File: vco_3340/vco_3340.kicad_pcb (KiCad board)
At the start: 2 copper layers, 55 x 95 mm, 44 parts, among them J1 cv1, J2 cv2, J3 FM in, J4 PWM, J5 Sync In, J6 Power In, J7 Pulse Out, J8 Saw Out, J9 Tri Out, U1 TL072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

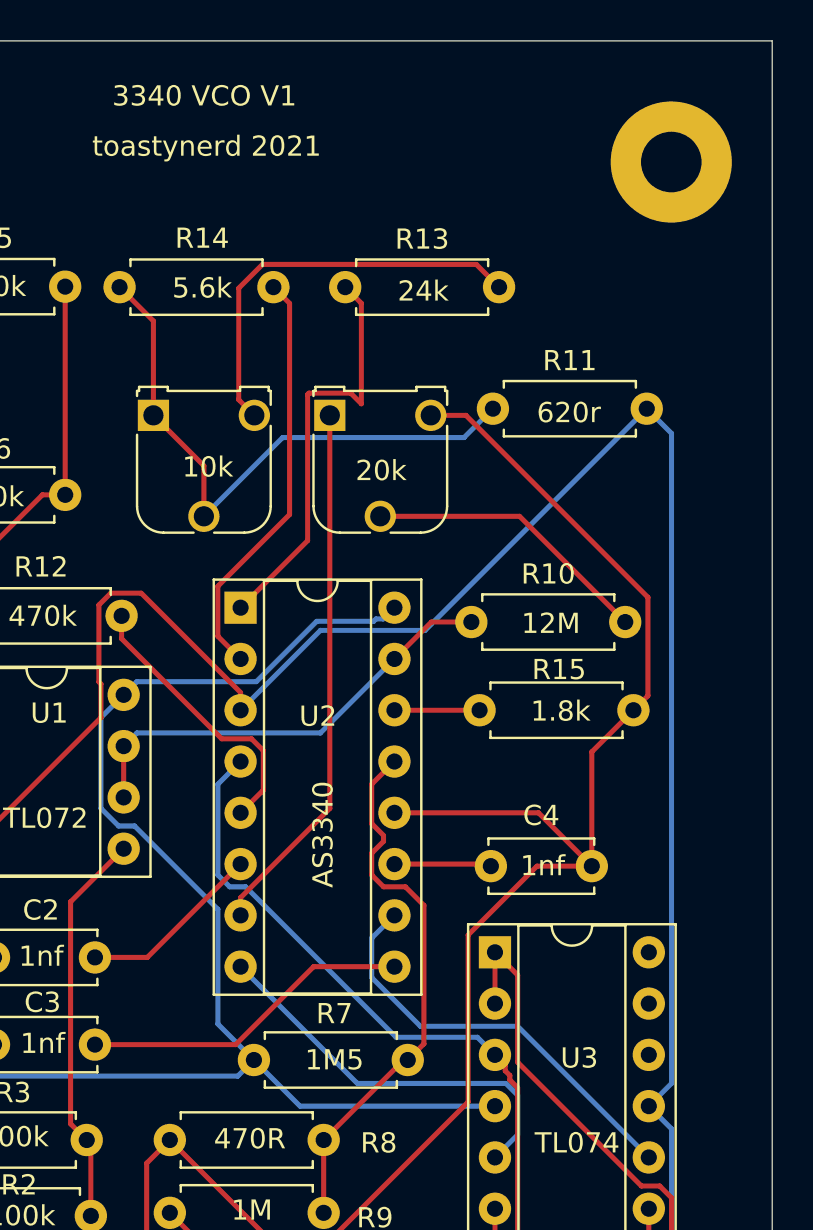
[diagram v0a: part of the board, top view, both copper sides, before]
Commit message: 3360 stencil and 3340 fixes
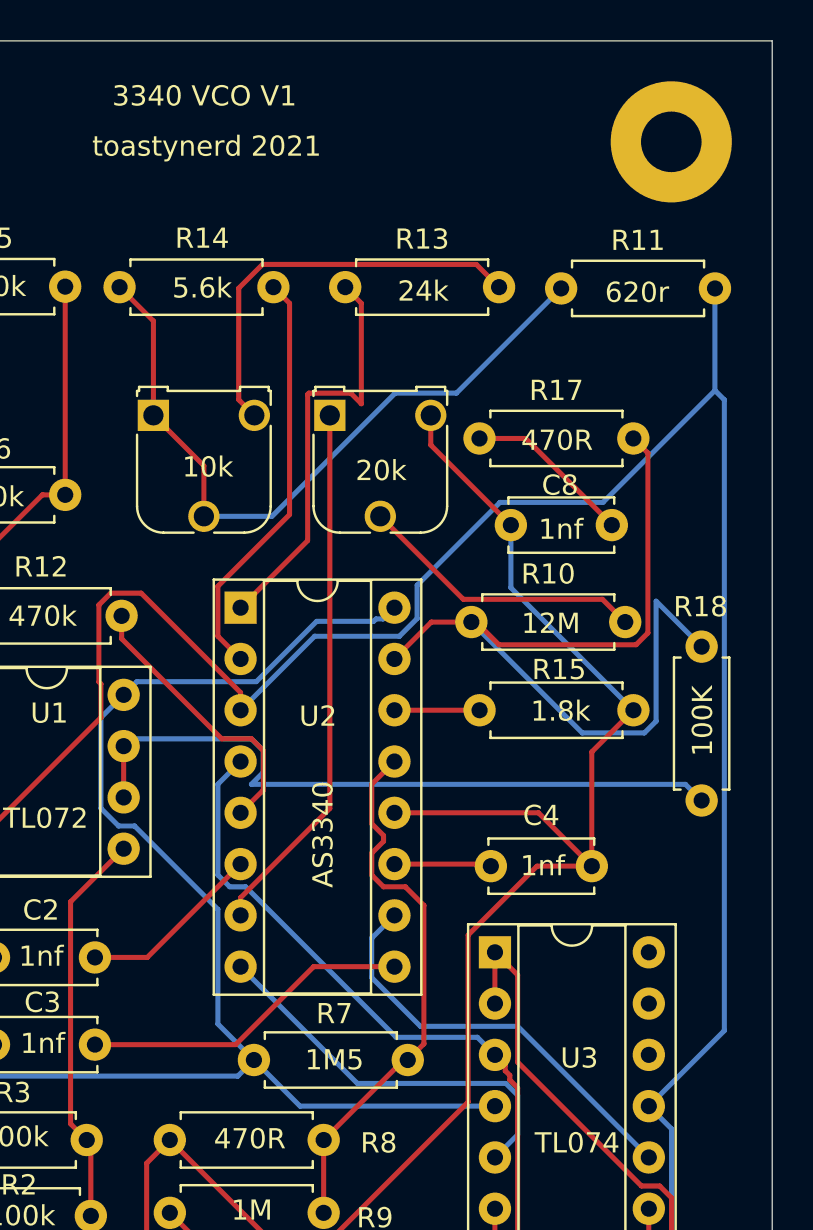
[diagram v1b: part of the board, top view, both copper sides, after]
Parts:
- added C8: 1nf, Capacitor_THT:C_Disc_D5.0mm_W2.5mm_P5.00mm, F.Cu at (132.1, 64.0)
- added R17: 470R, Resistor_THT:R_Axial_DIN0207_L6.3mm_D2.5mm_P7.62mm_Horizontal, F.Cu at (130.5, 59.7)
- added R18: 100K, Resistor_THT:R_Axial_DIN0207_L6.3mm_D2.5mm_P7.62mm_Horizontal, F.Cu at (141.5, 70.0)
- moved R11 6.85 mm to (134.5, 52.3)
- moved REF** 1.00 mm to (140.0, 45.0)
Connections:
- U1 pad 6: Net-(R10-Pad1) -> Net-(R18-Pad2)
- U1 pad 7: Net-(R10-Pad1) -> Net-(R18-Pad2)
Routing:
- net Net-(R18-Pad2): track 0.00 -> 34.4 mm
- net Net-(R10-Pad1): track 22.3 -> 44.8 mm
- net -12V: track 135.4 -> 146.8 mm
- net Net-(C8-Pad2): track 0.00 -> 8.35 mm
- net Net-(R11-Pad1): track 29.6 -> 35.4 mm
- net GND: track 250.3 -> 248.7 mm

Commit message: three new modules with pcbs
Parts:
- added C9: 10uf, Capacitor_THT:CP_Radial_D5.0mm_P2.00mm, F.Cu at (101.1, 129.0)
- added U4: L7805, Package_TO_SOT_THT:TO-220-3_Vertical, F.Cu at (98.5, 117.2)
- J6: footprint Connector_PinHeader_2.54mm:PinHeader_1x04_P2.54mm_Vertical -> Connector_PinHeader_2.54mm:PinHeader_1x03_P2.54mm_Vertical
- moved C7 18.5 mm to (109.8, 129.2)
- moved J6 2.03 mm to (106.8, 120.3)
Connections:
- C7 pad 1: +5V -> +12V
- U2 pad 3: -12V -> Net-(R11-Pad1)
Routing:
- net +12V: track 98.8 -> 129.2 mm
- net GND: track 248.7 -> 273.0 mm
- net Net-(R11-Pad1): track 35.4 -> 46.7 mm
- net +5V: track 82.5 -> 72.8 mm
- net -12V: track 146.8 -> 151.8 mm
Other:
- board text added: "3340 VCO V2"
- board text added: "JLCJLCJLCJLC"
- board text removed: "3340 VCO V1"
